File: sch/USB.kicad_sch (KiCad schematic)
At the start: 16 parts, among them U4 CH340N, X1 GT-TF003-H0185-02

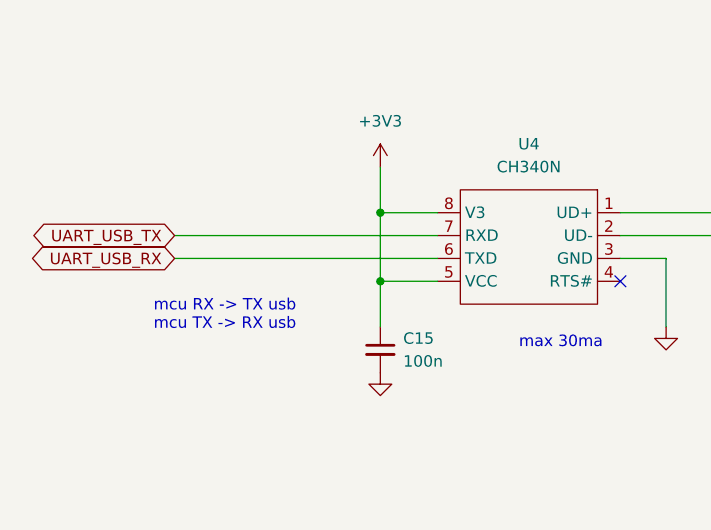
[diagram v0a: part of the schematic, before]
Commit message: Fix SPI pins add 3.3v led
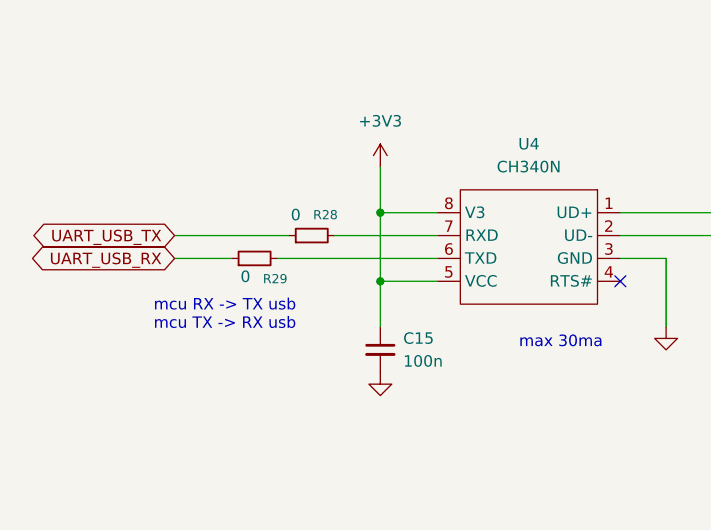
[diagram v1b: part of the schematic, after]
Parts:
- added R28, R29: 0, EasyEDA_Lib:R0603, symbol Device:R_Small
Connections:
- net UART_USB_RX: now also R29.1; no longer U4.6 (TXD)
- net UART_USB_TX: now also R28.1; no longer U4.7 (RXD)
- new net: R29.2, U4.6 (TXD)
- new net: R28.2, U4.7 (RXD)
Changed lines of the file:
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@@
 	(wire
 		(pts
-			(xy 74.93 53.34) (xy 104.14 53.34)
+			(xy 74.93 53.34) (xy 87.63 53.34)
 		)
 		(stroke
@@
 	(wire
 		(pts
+			(xy 92.71 53.34) (xy 104.14 53.34)
+		)
+		(stroke
+			(width 0)
+			(type default)
+		)
+	)
+	(wire
+		(pts
 			(xy 124.46 53.34) (xy 149.86 53.34)
 		)
@@
 	(wire
 		(pts
-			(xy 74.93 55.88) (xy 104.14 55.88)
+			(xy 74.93 55.88) (xy 81.28 55.88)
 		)
 		(stroke
@@
 	(wire
 		(pts
+			(xy 86.36 55.88) (xy 104.14 55.88)
+		)
+		(stroke
+			(width 0)
+			(type default)
+		)
+	)
+	(wire
+		(pts
 			(xy 149.86 132.08) (xy 130.81 132.08)
 		)
@@
 	)
 	(symbol
+		(lib_id "Device:R_Small")
+		(at 83.82 55.88 90)
+		(unit 1)
+		(exclude_from_sim no)
+		(in_bom yes)
+		(on_board yes)
+		(dnp no)
+		(property "Reference" "R29"
+			(at 86.106 58.166 90)
+			(effects
+				(font
+					(size 1.016 1.016)
+				)
+			)
+		)
+		(property "Value" "0"
+			(at 82.804 57.912 90)
+			(effects
+				(font
+					(size 1.27 1.27)
+				)
+			)
+		)
+		(property "Footprint" "EasyEDA_Lib:R0603"
+			(at 83.82 55.88 0)
+			(effects
+				(font
+					(size 1.27 1.27)
+				)
+				(hide yes)
+			)
+		)
+		(property "Datasheet" "https://jlcpcb.com/api/file/downloadByFileSystemAccessId/8578255895094087680"
+			(at 83.82 55.88 0)
+			(effects
+				(font
+					(size 1.27 1.27)
+				)
+				(hide yes)
+			)
+		)
+		(property "Description" "-55℃~+155℃ 0Ω 100mW 75V Thick Film Resistor ±1% 0603 Chip Resistor - Surface Mount ROHS"
+			(at 83.82 55.88 0)
+			(effects
+				(font
+					(size 1.27 1.27)
+				)
+				(hide yes)
+			)
+		)
+		(property "Supplier" "LCSC"
+			(at 83.82 55.88 0)
+			(effects
+				(font
+					(size 1.27 1.27)
+				)
+				(hide yes)
+			)
+		)
+		(property "Supplier Part" "C21189"
+			(at 83.82 55.88 0)
+			(effects
+				(font
+					(size 1.27 1.27)
+				)
+				(hide yes)
+			)
+		)
+		(pin "1"
+		)
+		(pin "2"
+		)
+		(instances
+			(project "canlogger"
+				(path "/c59a6287-5b72-492b-aa01-526032899224/6ef1d395-aa53-4e7a-8e4b-b7828baf3fc4"
+					(reference "R29")
+					(unit 1)
+				)
+			)
+		)
+	)
+	(symbol
 		(lib_id "power:GND")
 		(at 129.54 63.5 0)
@@
 					(unit 1)
 				)
+			)
+		)
+	)
+	(symbol
+		(lib_id "Device:R_Small")
+		(at 90.17 53.34 90)
+		(unit 1)
+		(exclude_from_sim no)
+		(in_bom yes)
+		(on_board yes)
+		(dnp no)
+		(property "Reference" "R28"
+			(at 91.694 51.054 90)
+			(effects
+				(font
+					(size 1.016 1.016)
+				)
+			)
+		)
+		(property "Value" "0"
+			(at 88.392 51.054 90)
+			(effects
+				(font
+					(size 1.27 1.27)
+				)
+			)
+		)
+		(property "Footprint" "EasyEDA_Lib:R0603"
+			(at 90.17 53.34 0)
+			(effects
+				(font
+					(size 1.27 1.27)
+				)
+				(hide yes)
+			)
+		)
+		(property "Datasheet" "https://jlcpcb.com/api/file/downloadByFileSystemAccessId/8578255895094087680"
+			(at 90.17 53.34 0)
+			(effects
+				(font
+					(size 1.27 1.27)
+				)
+				(hide yes)
+			)
+		)
+		(property "Description" "-55℃~+155℃ 0Ω 100mW 75V Thick Film Resistor ±1% 0603 Chip Resistor - Surface Mount ROHS"
+			(at 90.17 53.34 0)
+			(effects
+				(font
+					(size 1.27 1.27)
+				)
+				(hide yes)
+			)
+		)
+		(property "Supplier" "LCSC"
+			(at 90.17 53.34 0)
+			(effects
+				(font
+					(size 1.27 1.27)
+				)
+				(hide yes)
+			)
+		)
+		(property "Supplier Part" "C21189"
+			(at 90.17 53.34 0)
+			(effects
+				(font
+					(size 1.27 1.27)
+				)
+				(hide yes)
+			)
+		)
+		(pin "1"
+		)
+		(pin "2"
+		)
+		(instances
+			(project "canlogger"
+				(path "/c59a6287-5b72-492b-aa01-526032899224/6ef1d395-aa53-4e7a-8e4b-b7828baf3fc4"
+					(reference "R28")
+					(unit 1)
+				)

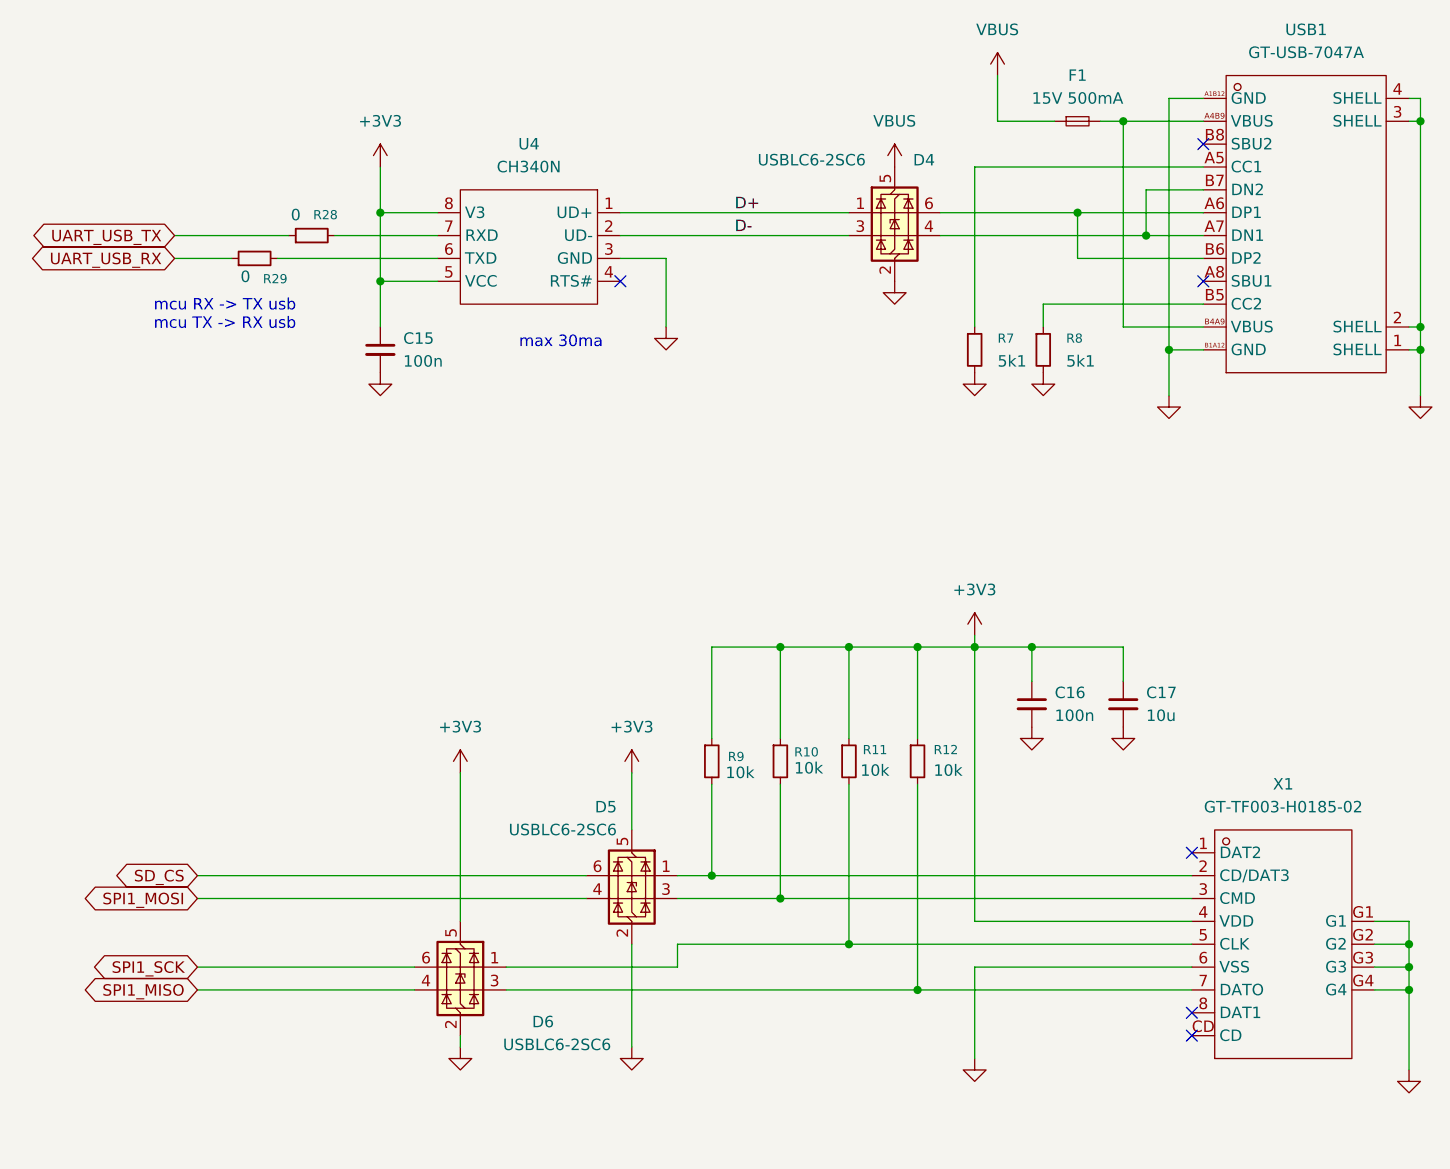
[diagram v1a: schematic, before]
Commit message: change 2x22u to 3x10u plot all order jlcpcb + lcsc
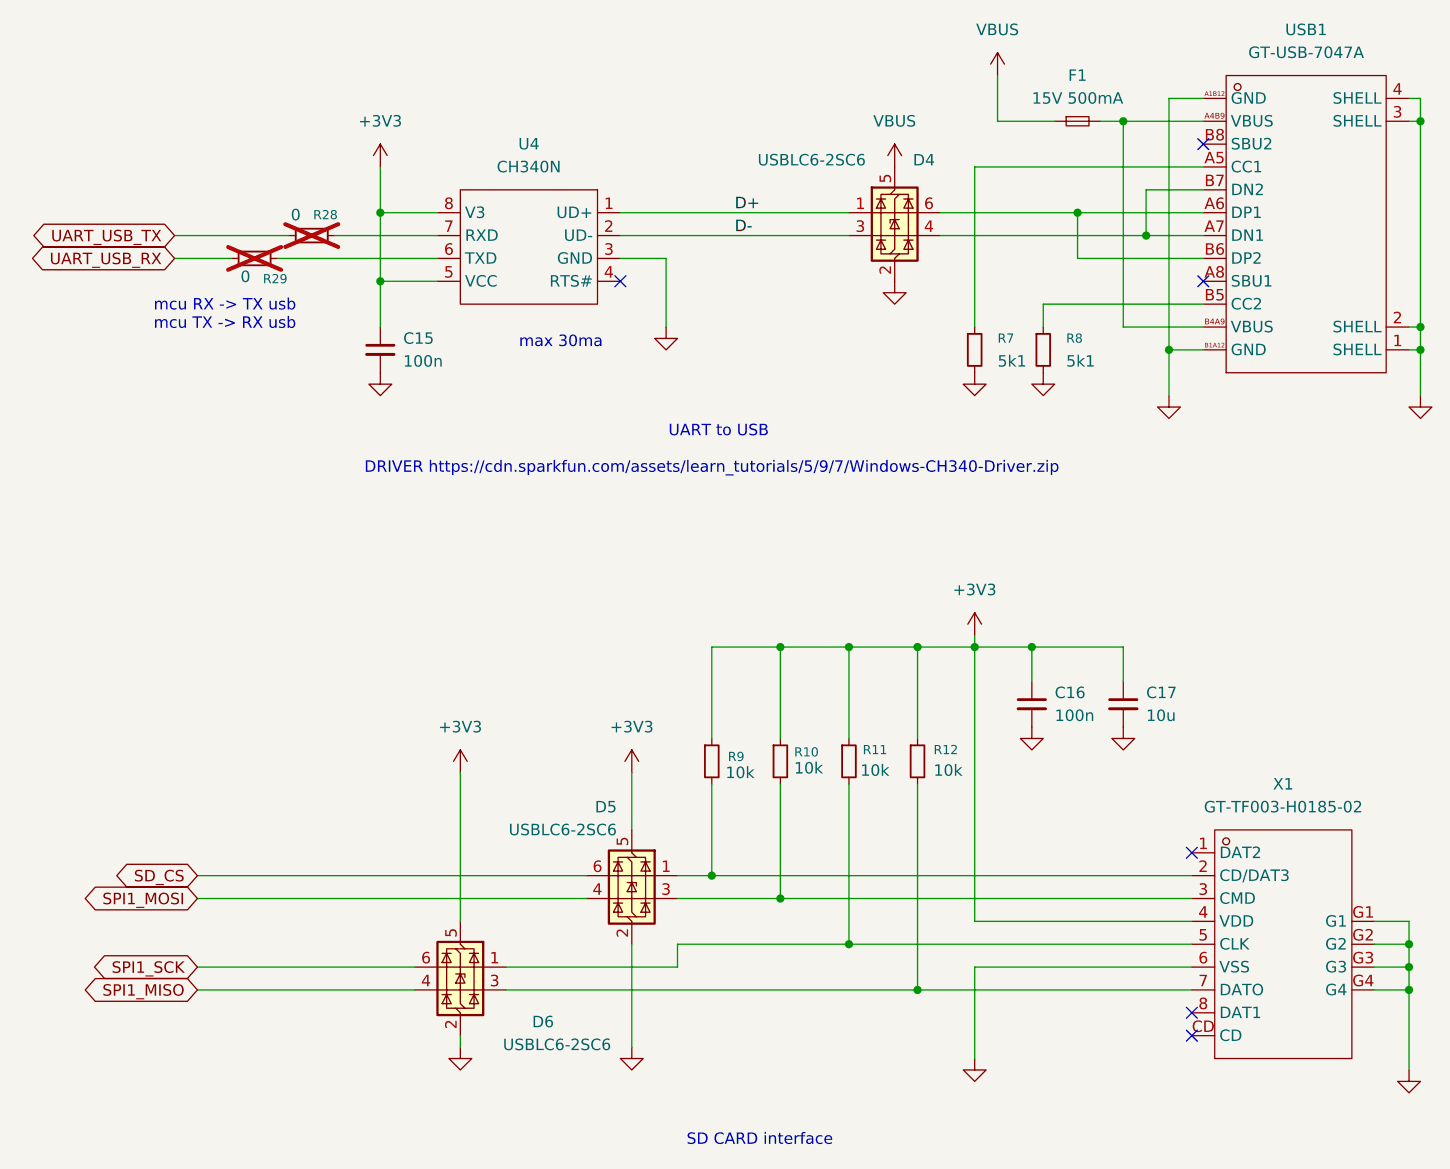
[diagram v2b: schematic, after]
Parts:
- R28, R29: now not fitted
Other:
- note added: "DRIVER https://cdn.sparkfun.com/assets/learn_tutorials/5/9/7/Windows-CH340-Driver.zip"
- note added: "SD CARD interface"
- note added: "UART to USB"
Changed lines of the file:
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@@
 		(rev "1.0")
 	)
+	(text "SD CARD interface"
+		(exclude_from_sim no)
+		(at 139.954 153.924 0)
+		(effects
+			(font
+				(size 1.27 1.27)
+			)
+		)
+	)
+	(text "DRIVER https://cdn.sparkfun.com/assets/learn_tutorials/5/9/7/Windows-CH340-Driver.zip"
+		(exclude_from_sim no)
+		(at 134.62 79.248 0)
+		(effects
+			(font
+				(size 1.27 1.27)
+			)
+		)
+	)
 	(text "max 30ma"
 		(exclude_from_sim no)
@@
 		)
 	)
+	(text "UART to USB\n"
+		(exclude_from_sim no)
+		(at 135.382 75.184 0)
+		(effects
+			(font
+				(size 1.27 1.27)
+			)
+		)
+	)
 	(junction
 		(at 157.48 99.06)
@@
 		(in_bom yes)
 		(on_board yes)
-		(dnp no)
+		(dnp yes)
 		(property "Reference" "R29"
 			(at 86.106 58.166 90)
@@
 		(in_bom yes)
 		(on_board yes)
-		(dnp no)
+		(dnp yes)
 		(property "Reference" "R28"
 			(at 91.694 51.054 90)
